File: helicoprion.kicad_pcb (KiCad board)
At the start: 2 copper layers, 134.5 x 126 mm, 53 parts, among them J1 TRRS, J2 TRRS, SW1 SW_SPST, SW10 SW_SPST, SW11 SW_SPST, SW12 SW_SPST, SW13 SW_SPST, SW14 SW_SPST, SW15 SW_SPST, SW16 SW_SPST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

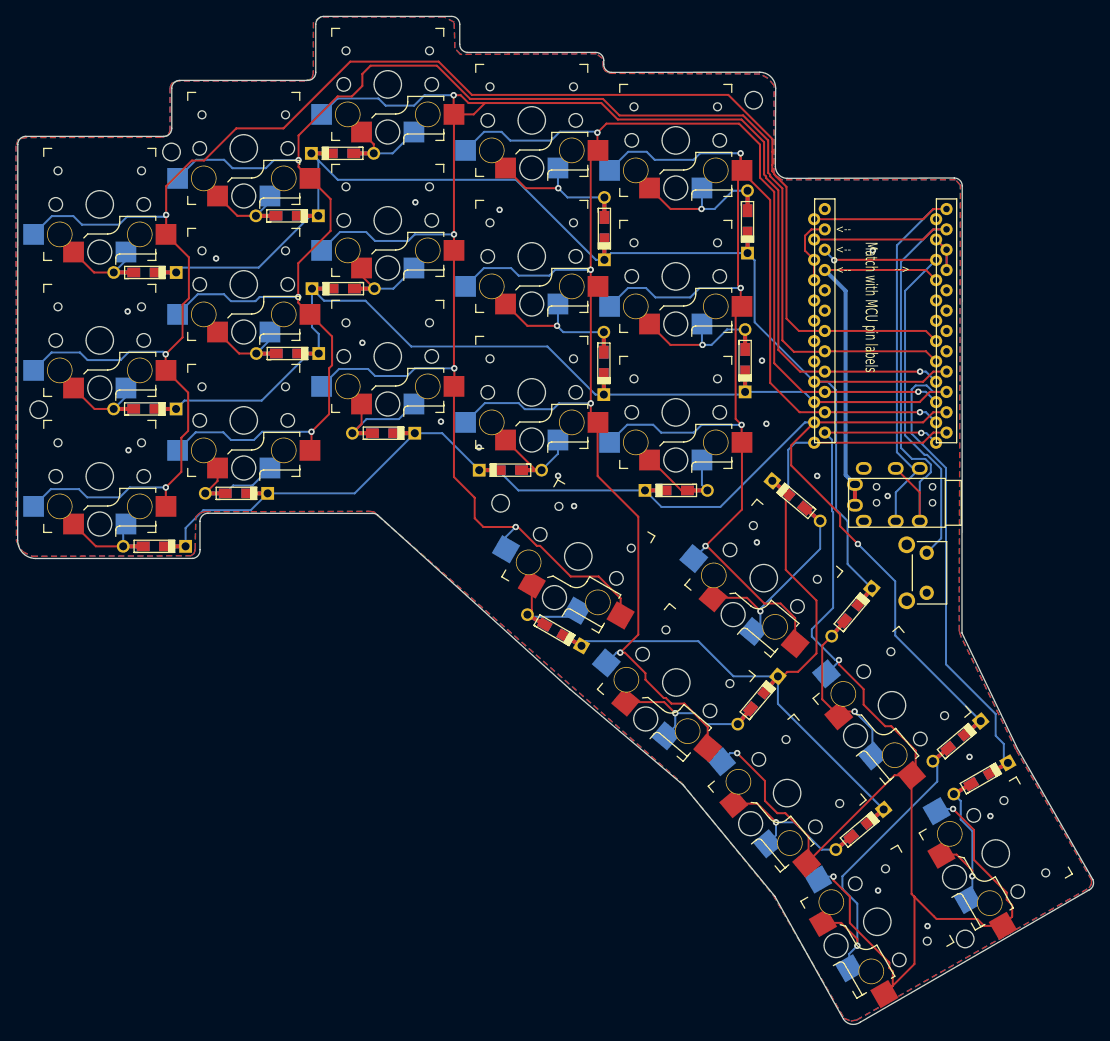
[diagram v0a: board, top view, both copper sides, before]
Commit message: start of firmware and interactive bom
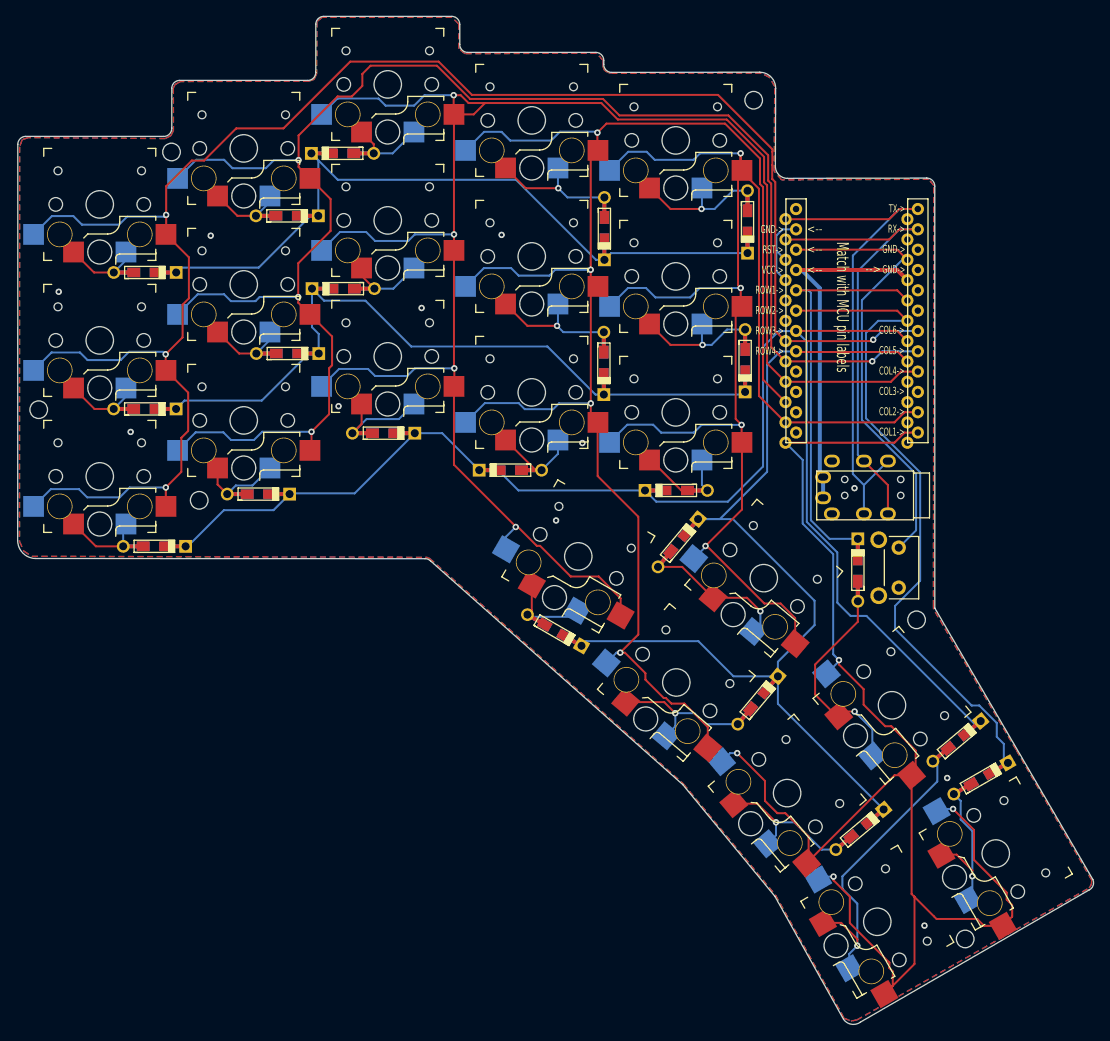
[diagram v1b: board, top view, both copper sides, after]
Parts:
- added H6: MountingHole, MountingHole:MountingHole_2.2mm_M2, F.Cu at (173.6, 97.9)
- moved H4 37.7 mm to (83.9, 83.0)
- moved D6 15.7 mm to (143.8, 88.3), turned to 50 degrees
- moved D3 5.33 mm to (166.3, 91.7), turned to 90 degrees
- moved J1 4.08 mm to (173.2, 82.4)
- moved J2 4.08 mm to (173.2, 80.4)
- moved U1 3.59 mm to (166.1, 61.1)
- moved RSW1 3.56 mm to (170.1, 91.4)
- moved D20 2.74 mm to (91.3, 82.2)
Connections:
- U1 pad 10: row2 -> col3
- U1 pad 11: row3 -> col2
- U1 pad 12: row4 -> col1
- U1 pad 13: col1 -> unconnected-(U1-10/B6-Pad13)
- U1 pad 14: col2 -> unconnected-(U1-16/B2-Pad14)
- U1 pad 15: col3 -> unconnected-(U1-14/B3-Pad15)
- U1 pad 16: col4 -> unconnected-(U1-15/B1-Pad16)
- U1 pad 17: col5 -> row4
- U1 pad 18: col6 -> row3
- U1 pad 19: unconnected-(U1-A2/F5-Pad19) -> row2
- U1 pad 20: unconnected-(U1-A3/F4-Pad20) -> row1
- U1 pad 7: unconnected-(U1-D4/4-Pad7) -> col6
- U1 pad 8: unconnected-(U1-C6/5-Pad8) -> col5
- U1 pad 9: row1 -> col4
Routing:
- net row4: track 102.6 -> 121.8 mm
- net row3: track 159.4 -> 178.1 mm, vias 1 -> 0
- net col3: track 214.9 -> 197.1 mm, vias 5 -> 4
- net row1: track 155.7 -> 140.9 mm
- net rx: track 67.9 -> 58.6 mm
- net GND: track 17.6 -> 10.8 mm, vias 19 -> 11
- net Net-(D3-A): track 20.0 -> 26.6 mm
- net Net-(D6-A): track 23.9 -> 18.0 mm
- net col4: track 230.4 -> 227.0 mm, vias 5 -> 4
- net tx: track 62.6 -> 64.7 mm
- net row2: track 171.7 -> 173.4 mm
- net col5: track 210.9 -> 209.3 mm, vias 3 -> 4
- net reset: track 55.6 -> 56.9 mm, vias 1 -> 0
- net col6: track 229.2 -> 228.5 mm, vias 3 -> 4
- net col1: track 188.1 -> 188.8 mm, vias 5 -> 4
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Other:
- outline, holes or cut-outs redrawn

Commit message: new gerber and ibom
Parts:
- moved H1 16.7 mm to (63.8, 40.0)
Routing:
- net GND: track 10.8 -> 15.1 mm
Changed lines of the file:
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@@
   )
   (footprint "MountingHole:MountingHole_2.2mm_M2" (layer "F.Cu")
-    (at 80.47 39.45)
+    (at 63.8 40.05)
     (descr "Mounting Hole 2.2mm, no annular, M2")
     (tags "mounting hole 2.2mm no annular m2")
@@
   (gr_arc (start 98.5 23.5) (mid 98.792893 22.792893) (end 99.5 22.5)
     (stroke (width 0.1) (type default)) (layer "Edge.Cuts"))
+  (segment (start 172.49 50.39) (end 173.76 51.66) (width 0.25) (layer "F.Cu") (net 1))
+  (segment (start 172.4536 50.39) (end 172.49 50.39) (width 0.25) (layer "F.Cu") (net 1))
+  (segment (start 173.76 51.66) (end 173.76 54.2) (width 0.25) (layer "F.Cu") (net 1))
   (via (at 111.73 58.95) (size 0.8) (drill 0.4) (layers "F.Cu" "B.Cu") (free) (net 1))
   (via (at 85.37 49.91) (size 0.8) (drill 0.4) (layers "F.Cu" "B.Cu") (free) (net 1))

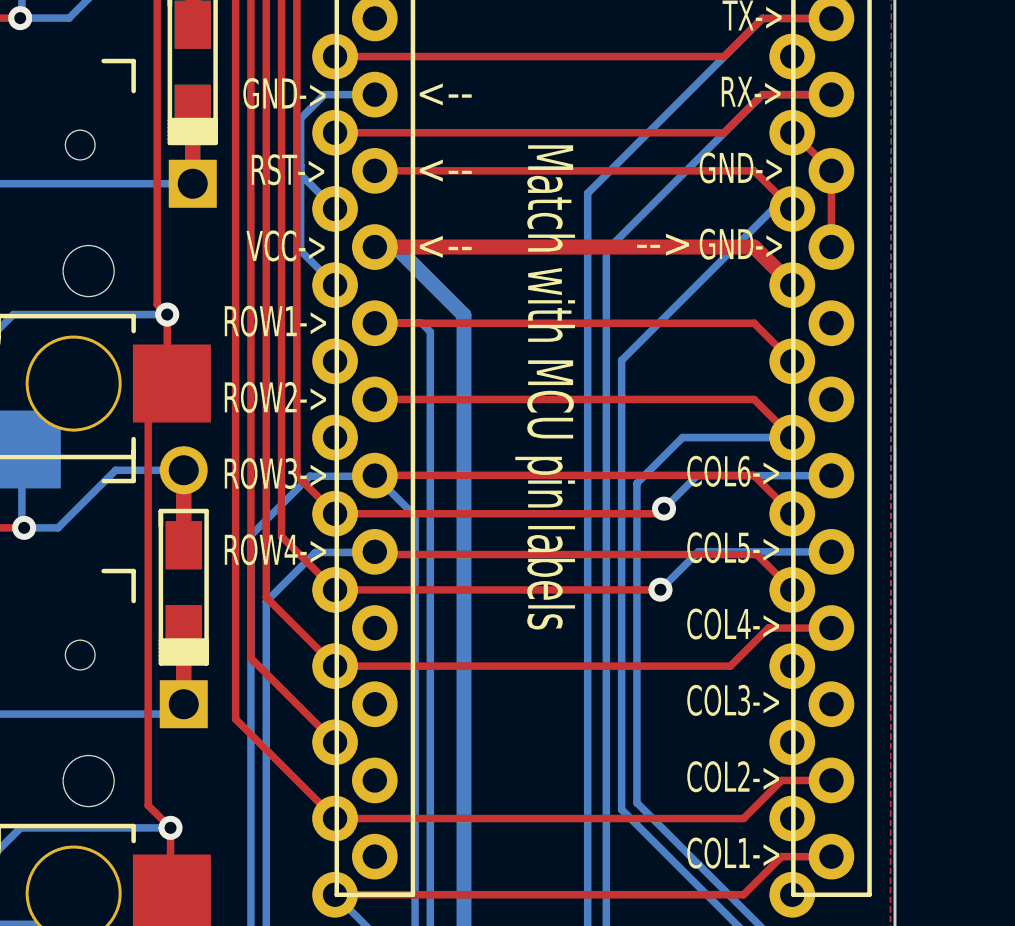
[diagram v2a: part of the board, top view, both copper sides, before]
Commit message: fix erata for v1 and get left side working
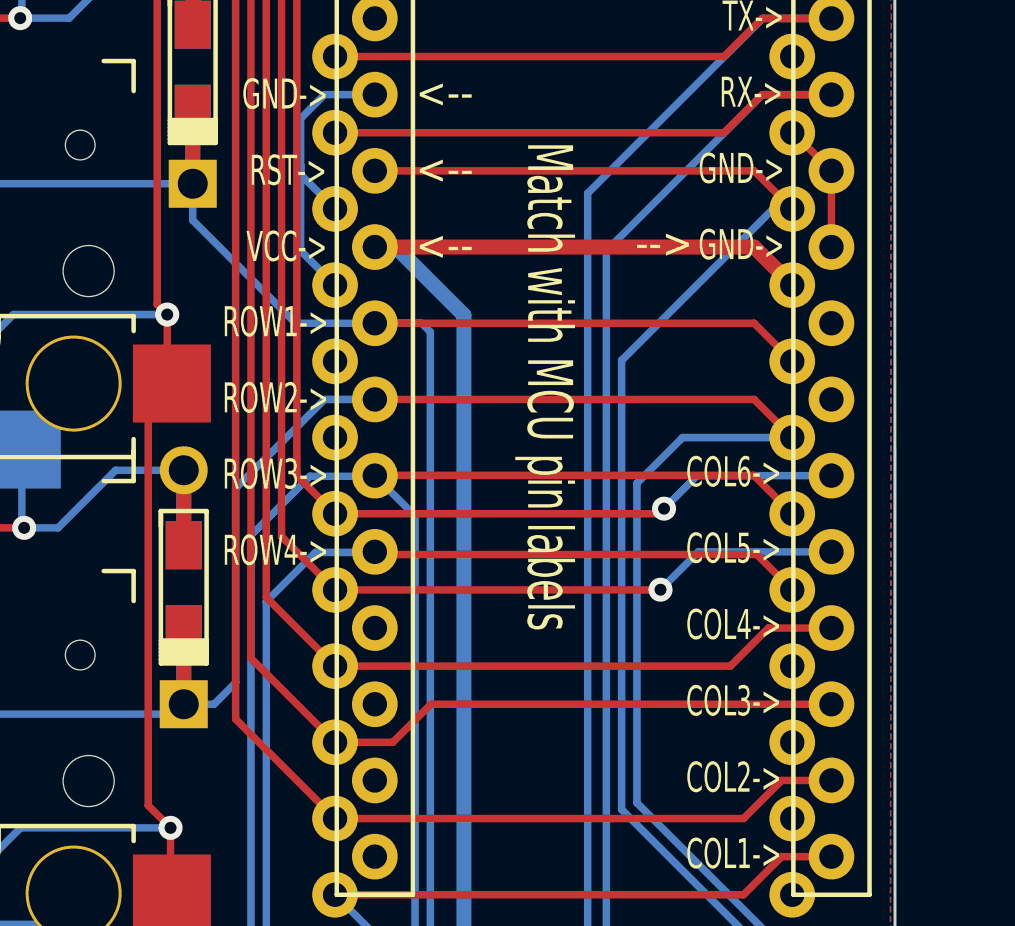
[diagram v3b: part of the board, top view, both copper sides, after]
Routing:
- net col3: track 197.1 -> 214.1 mm
- net row2: track 173.4 -> 187.8 mm
- net row1: track 140.9 -> 149.7 mm
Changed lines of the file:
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@@
   (segment (start 135.42 52.09) (end 152.47 52.09) (width 0.25) (layer "B.Cu") (net 5))
   (segment (start 123.5197 42.9197) (end 133.53 52.93) (width 0.25) (layer "B.Cu") (net 5))
+  (segment (start 152.47 52.09) (end 152.47 53.31) (width 0.25) (layer "B.Cu") (net 5))
   (segment (start 160.1 56.74) (end 158.54 56.74) (width 0.25) (layer "B.Cu") (net 5))
   (segment (start 134.58 52.93) (end 135.42 52.09) (width 0.25) (layer "B.Cu") (net 5))
   (segment (start 81.6595 53.9005) (end 91.374568 53.9005) (width 0.25) (layer "B.Cu") (net 5))
   (segment (start 160.39 57.03) (end 160.1 56.74) (width 0.25) (layer "B.Cu") (net 5))
+  (segment (start 155.9 56.74) (end 158.54 56.74) (width 0.25) (layer "B.Cu") (net 5))
   (segment (start 166.259693 87.806119) (end 162.716119 87.806119) (width 0.25) (layer "B.Cu") (net 5))
   (segment (start 97.845068 47.43) (end 98.82 47.43) (width 0.25) (layer "B.Cu") (net 5))
   (segment (start 91.374568 53.9005) (end 97.845068 47.43) (width 0.25) (layer "B.Cu") (net 5))
   (segment (start 98.82 47.43) (end 98.82 40.49) (width 0.25) (layer "B.Cu") (net 5))
+  (segment (start 152.47 53.31) (end 155.9 56.74) (width 0.25) (layer "B.Cu") (net 5))
   (segment (start 97.95 39.62) (end 101.2497 42.9197) (width 0.25) (layer "B.Cu") (net 5))
   (segment (start 142.835 63.56) (end 146.85 63.56) (width 0.25) (layer "F.Cu") (net 6))
@@
   (segment (start 154.41 43.832908) (end 154.41 67.9064) (width 0.25) (layer "F.Cu") (net 26))
   (segment (start 132.87 54.17) (end 132.87 55.345) (width 0.25) (layer "F.Cu") (net 26))
+  (segment (start 173.76 69.44) (end 160.408103 69.44) (width 0.25) (layer "F.Cu") (net 26))
   (segment (start 139.71 105.41) (end 139.71 104.6) (width 0.25) (layer "F.Cu") (net 26))
   (segment (start 133.71 37.03) (end 134.8395 35.9005) (width 0.25) (layer "F.Cu") (net 26))
@@
   (segment (start 147.498564 111.318564) (end 144.58 108.4) (width 0.25) (layer "F.Cu") (net 26))
   (segment (start 133.735 79.955) (end 133.735 73.29) (width 0.25) (layer "F.Cu") (net 26))
+  (segment (start 160.408103 69.44) (end 159.138103 70.71) (width 0.25) (layer "F.Cu") (net 26))
   (segment (start 134.8395 35.9005) (end 149.6605 35.9005) (width 0.25) (layer "F.Cu") (net 26))
   (segment (start 149.6605 35.9005) (end 154.029172 40.269172) (width 0.25) (layer "F.Cu") (net 26))
@@
   (segment (start 132.88 57.145) (end 133.775 56.25) (width 0.25) (layer "F.Cu") (net 26))
   (segment (start 142.961248 108.4) (end 142.264083 107.702835) (width 0.25) (layer "F.Cu") (net 26))
+  (segment (start 159.138103 70.71) (end 157.2136 70.71) (width 0.25) (layer "F.Cu") (net 26))
   (segment (start 154.41 67.9064) (end 157.2136 70.71) (width 0.25) (layer "F.Cu") (net 26))
   (segment (start 154.029172 43.45208) (end 154.41 43.832908) (width 0.25) (layer "F.Cu") (net 26))
@@
   (segment (start 167.27705 62.07295) (end 168.8 60.55) (width 0.25) (layer "B.Cu") (net 31))
   (segment (start 91.755068 70.52) (end 97.635068 64.64) (width 0.25) (layer "B.Cu") (net 31))
+  (segment (start 156.861497 59.28) (end 158.54 59.28) (width 0.25) (layer "B.Cu") (net 31))
   (segment (start 98.03 61.35) (end 98.03 56.53) (width 0.25) (layer "B.Cu") (net 31))
   (segment (start 180.485411 108.635411) (end 170.91 99.06) (width 0.25) (layer "B.Cu") (net 31))
   (segment (start 151.84 69.77) (end 152.17 69.44) (width 0.25) (layer "B.Cu") (net 31))
+  (segment (start 152.17 69.44) (end 153.18 69.44) (width 0.25) (layer "B.Cu") (net 31))
   (segment (start 98.87 62.19) (end 98.03 61.35) (width 0.25) (layer "B.Cu") (net 31))
+  (segment (start 153.9 68.72) (end 153.9 62.241497) (width 0.25) (layer "B.Cu") (net 31))
   (segment (start 183.625 112.555) (end 183.625 110.820411) (width 0.25) (layer "B.Cu") (net 31))
   (segment (start 181.44 108.635411) (end 180.485411 108.635411) (width 0.25) (layer "B.Cu") (net 31))
   (segment (start 184.512046 115.304547) (end 184.512046 113.442046) (width 0.25) (layer "B.Cu") (net 31))
   (segment (start 170.91 99.06) (end 170.91 96.187265) (width 0.25) (layer "B.Cu") (net 31))
+  (segment (start 153.9 62.241497) (end 156.861497 59.28) (width 0.25) (layer "B.Cu") (net 31))
   (segment (start 98.03 56.53) (end 99.54 58.04) (width 0.25) (layer "B.Cu") (net 31))
   (segment (start 167.27705 72.72705) (end 167.27705 62.07295) (width 0.25) (layer "B.Cu") (net 31))
@@
   (segment (start 81.04 71.57) (end 82.09 70.52) (width 0.25) (layer "B.Cu") (net 31))
   (segment (start 97.635068 64.64) (end 98.87 64.64) (width 0.25) (layer "B.Cu") (net 31))
+  (segment (start 153.18 69.44) (end 153.9 68.72) (width 0.25) (layer "B.Cu") (net 31))
   (segment (start 170.91 96.187265) (end 174.05 93.047265) (width 0.25) (layer "B.Cu") (net 31))
   (segment (start 185.017499 115.81) (end 184.512046 115.304547) (width 0.25) (layer "B.Cu") (net 31))
